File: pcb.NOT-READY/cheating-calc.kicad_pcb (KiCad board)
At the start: 2 copper layers, 72 x 22 mm, 16 parts, among them J1 Conn_01x04, J2 Conn_01x04, Q1 MMBF170, Q2 MMBF170, U2 SE5218ALG-LF, U3 ESP32-C3-MINI-1-N4

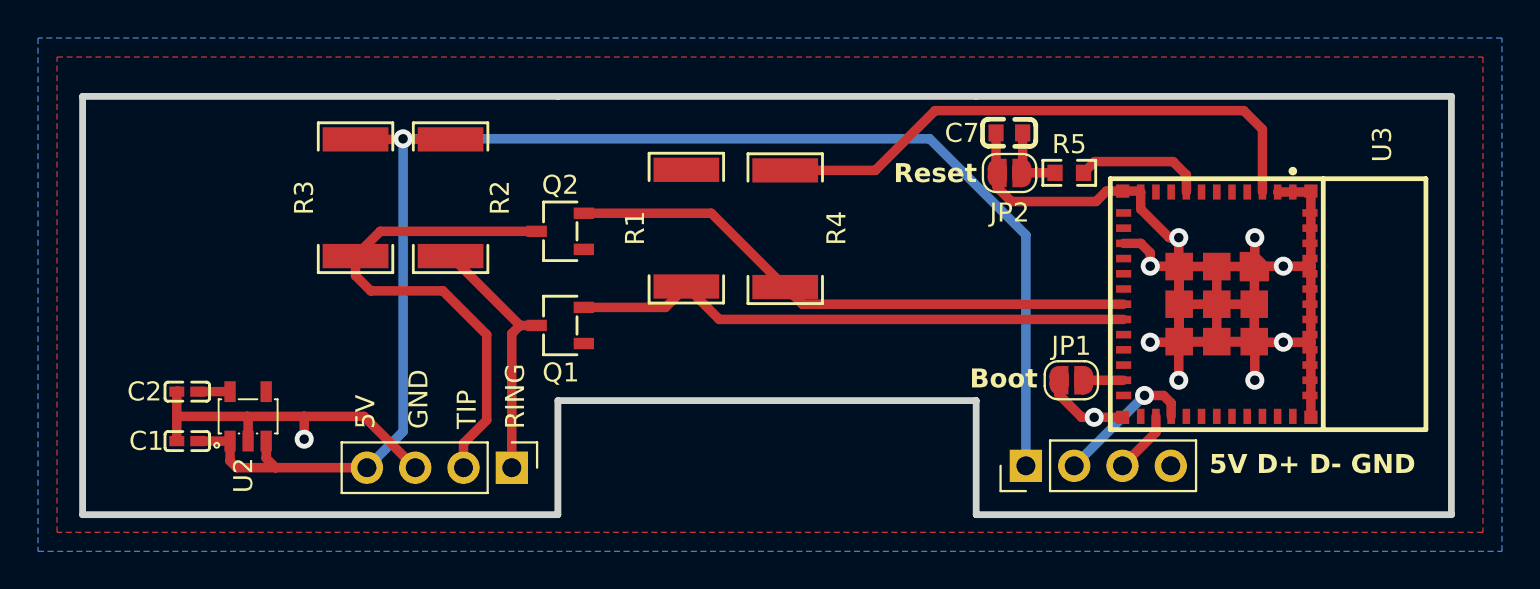
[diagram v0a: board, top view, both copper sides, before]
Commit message: update LDO regulator to be a genuine TI (and add redundency for other versions in schem)
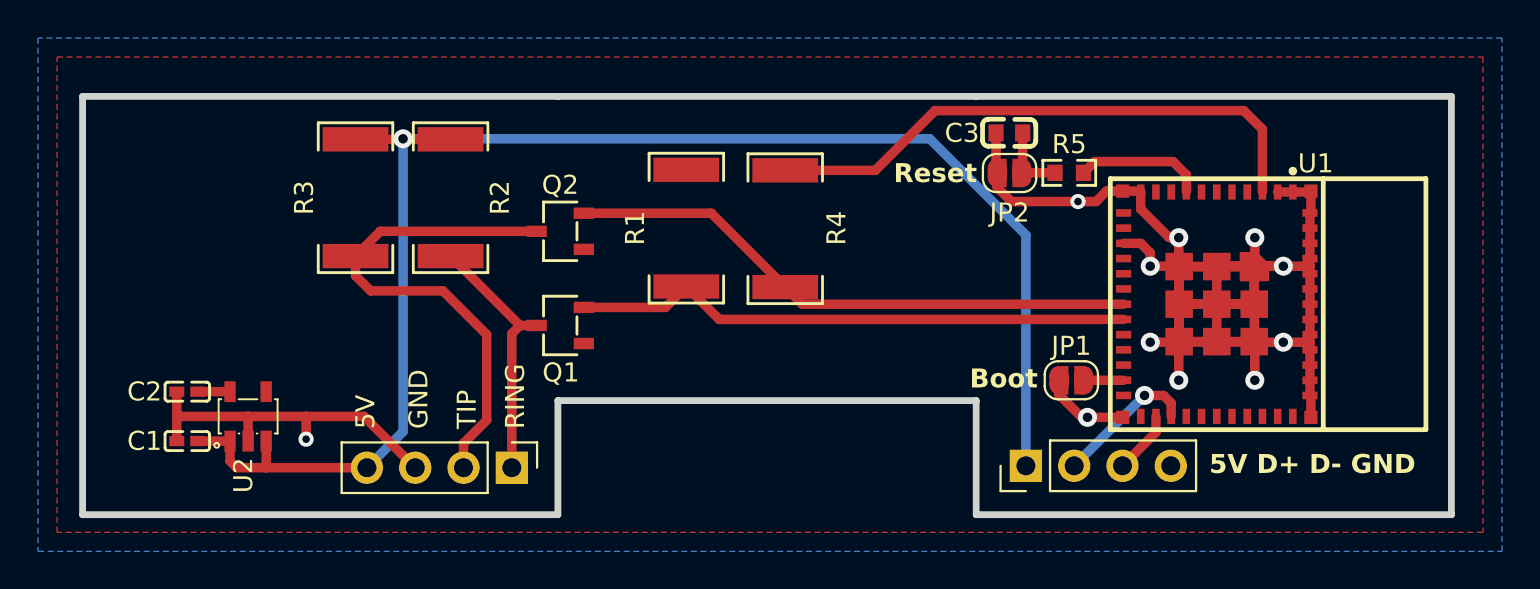
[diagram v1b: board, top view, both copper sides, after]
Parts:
- C1, C2: value GRM155R61A225KE95D -> CL05A105KP5NNNC
- U2: value SE5218ALG-LF -> TLV75533PDBVR
- turned C1 to 180 degrees
- turned C2 to 180 degrees
- renumbered C7 to C3, U3 to U1
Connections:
- C1 pad 1: GND -> +5V
- C1 pad 2: +5V -> GND
- C2 pad 1: GND -> +3.3V
- C2 pad 2: +3.3V -> GND
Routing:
- net GND: track 101.6 -> 114.9 mm, vias 10 -> 11

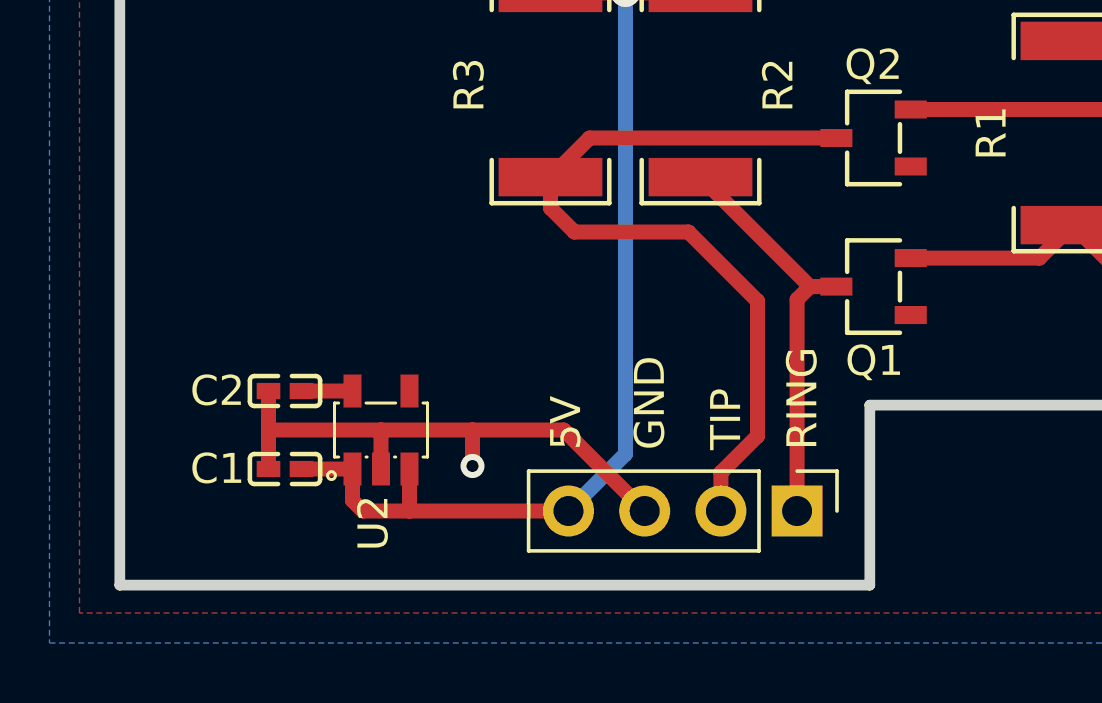
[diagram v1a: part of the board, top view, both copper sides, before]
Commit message: Update regulator chip and remove rounded versions
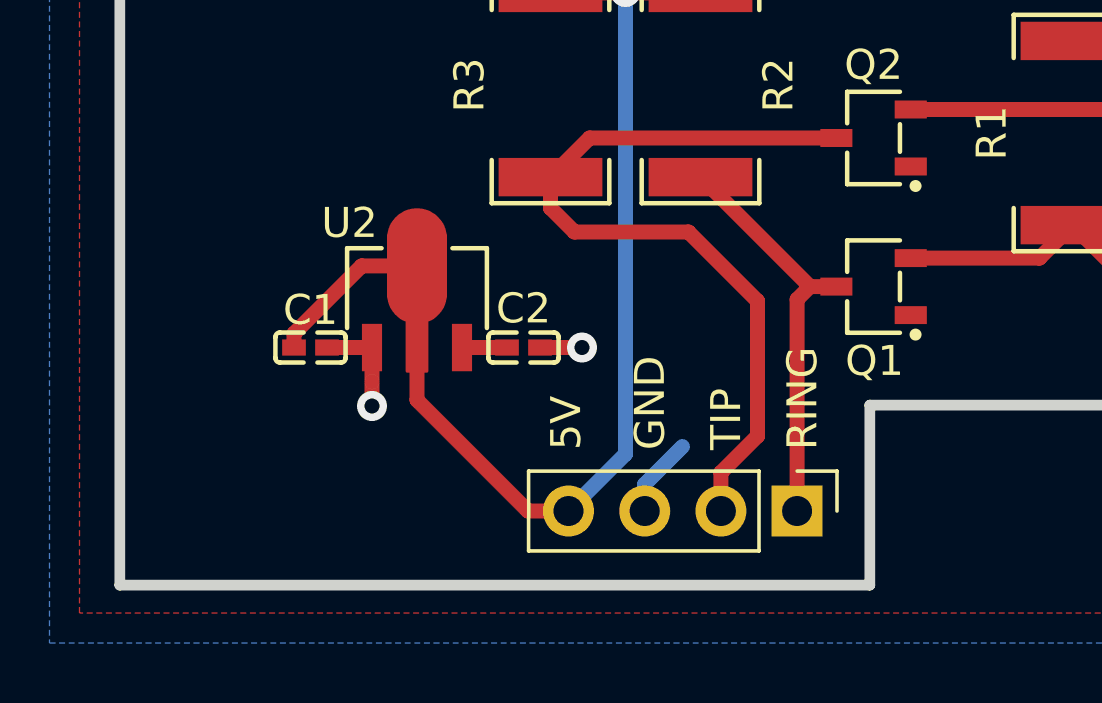
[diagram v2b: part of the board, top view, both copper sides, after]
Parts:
- U2: value TLV75533PDBVR -> AP7215-33YG-13; footprint easyeda2kicad:SOT-23-5_L3.0-W1.7-P0.95-LS2.8-BR -> easyeda2kicad:SOT-89-3_L4.5-W2.5-P1.50-LS4.2-BR
- moved C2 8.08 mm to (98.8, 66.2), turned to 0 degrees
- moved U2 4.28 mm to (95.2, 64.8)
- moved C1 4.14 mm to (91.7, 66.2), turned to 0 degrees
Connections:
- U2 pad 1: +5V -> GND
- U2 pad 2: GND -> +5V
- U2 pad 3: +5V -> +3.3V
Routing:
- net GND: track 114.9 -> 103.6 mm, vias 11 -> 12
- net +5V: track 81.6 -> 86.7 mm

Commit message: update routing
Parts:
- C1, C2: value CL05A105KP5NNNC -> CL21B105KBFNNNE; footprint easyeda2kicad:C0402 -> easyeda2kicad:C0805
- moved C2 3.72 mm to (95.2, 65.0), turned to 90 degrees
- moved C1 3.63 mm to (88.2, 65.0), turned to -90 degrees
- moved U2 3.54 mm to (91.8, 64.3)
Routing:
- net +5V: track 86.7 -> 88.8 mm
- net GND: track 103.6 -> 105.2 mm
- net +3.3V: track 31.6 -> 32.3 mm
